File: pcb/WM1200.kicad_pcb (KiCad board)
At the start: 2 copper layers, 159 x 104 mm, 142 parts, among them Q1 BC817, Q2 BC817, Q3 BC817, Q4 BC817, Q5 BC817, Q6 BC817, U1 74LVCH162245A, U2 74LVCH162245A, U3 74LVCH162245A, U4 74LVCH162245A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

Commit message: working on pcb
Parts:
- moved X3 86.6 mm to (35.0, 118.7)
- moved XT10 77.0 mm to (189.0, 35.3)
- moved XT12 77.0 mm to (189.0, 36.8)
- moved XT14 77.0 mm to (189.0, 38.3)
- moved XT16 77.0 mm to (189.0, 39.8)
- moved XT18 77.0 mm to (189.0, 41.3)
- moved XT20 77.0 mm to (189.0, 42.8)
- moved XT6 77.0 mm to (189.0, 32.3)
- moved XT8 77.0 mm to (189.0, 33.8)
- moved U4 74.4 mm to (179.8, 42.5)
- moved XT11 73.9 mm to (170.0, 36.8)
- moved XT13 73.9 mm to (170.0, 38.3)
- moved XT15 73.9 mm to (170.0, 39.8)
- moved XT17 73.9 mm to (170.0, 41.3)
- moved XT19 73.9 mm to (170.0, 42.8)
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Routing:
- net GND: track 0.00 -> 57.5 mm
- net Net-(U5-Pad13): track 0.00 -> 19.0 mm
- net Net-(U5-Pad36): track 0.00 -> 18.9 mm, vias 0 -> 2
- net Net-(U5-Pad35): track 0.00 -> 18.8 mm, vias 0 -> 2
- net Net-(U5-Pad14): track 0.00 -> 18.6 mm
- net Net-(U5-Pad26): track 0.00 -> 9.89 mm
- net Net-(U5-Pad23): track 0.00 -> 9.85 mm
- net Net-(U5-Pad27): track 0.00 -> 8.97 mm
- net Net-(U5-Pad22): track 0.00 -> 8.90 mm
- net Net-(U5-Pad29): track 0.00 -> 8.71 mm
- net D0: track 0.00 -> 8.59 mm
- net D1: track 0.00 -> 8.57 mm
- net D2: track 0.00 -> 8.34 mm
- net D3: track 0.00 -> 8.32 mm
- net Net-(U5-Pad20): track 0.00 -> 8.32 mm
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
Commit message: working on pcb
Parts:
- moved U4 71.6 mm to (125.5, 89.2)
- moved XT11 71.6 mm to (115.8, 83.6)
- moved XT13 71.6 mm to (115.8, 85.1)
- moved XT15 71.6 mm to (115.8, 86.6)
- moved XT17 71.6 mm to (115.8, 88.1)
- moved XT19 71.6 mm to (115.8, 89.6)
- moved XT5 71.6 mm to (115.8, 79.1)
- moved XT7 71.6 mm to (115.8, 80.6)
- moved XT9 71.6 mm to (115.8, 82.1)
- moved XT10 71.6 mm to (134.8, 82.1)
- moved XT12 71.6 mm to (134.8, 83.6)
- moved XT14 71.6 mm to (134.8, 85.1)
- moved XT16 71.6 mm to (134.8, 86.6)
- moved XT18 71.6 mm to (134.8, 88.1)
- moved XT20 71.6 mm to (134.8, 89.6)
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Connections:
- XT11 pad 1: R_W -> _DS
- XT12 pad 2: FPGA_R_W -> _FPGA_DS
- XT13 pad 1: _DS -> R_W
- XT14 pad 2: _FPGA_DS -> FPGA_R_W
- XT17 pad 1: SIZE0 -> SIZE1
- XT18 pad 2: FPGA_SIZE0 -> FPGA_SIZE1
- XT19 pad 1: SIZE1 -> SIZE0
- XT20 pad 2: FPGA_SIZE1 -> FPGA_SIZE0
- XT37 pad 1: _IPL2 -> _IPL1
- XT38 pad 2: _FPGA_IPL2 -> _FPGA_IPL1
- XT39 pad 1: _IPL1 -> _IPL2
- XT40 pad 2: _FPGA_IPL1 -> _FPGA_IPL2
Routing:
- net _KBRESET: track 0.00 -> 25.7 mm
- net D18: track 0.00 -> 19.7 mm
- net A6: track 0.00 -> 19.6 mm
- net D24: track 0.00 -> 19.5 mm
- net D28: track 0.00 -> 19.3 mm
- net D8: track 0.00 -> 19.3 mm
- net D22: track 0.00 -> 19.2 mm
- net A18: track 0.00 -> 19.2 mm
- net D12: track 0.00 -> 19.1 mm
- net A2: track 0.00 -> 19.1 mm
- net A22: track 0.00 -> 19.0 mm
- net A12: track 0.00 -> 19.0 mm
- net A8: track 0.00 -> 18.9 mm
- net FC1: track 0.00 -> 13.9 mm
- net _DS: track 0.00 -> 13.0 mm
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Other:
- copper layers 2 -> 4

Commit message: Board pcb updated
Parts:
- removed XT1, XT2, XT3, XT4: testpoint, WM1200:testpoint
- removed XT53, XT54: testpoint_cutline, WM1200:testpoint_cutline
- C1, C2, C5, C9, R3, R4, R5, R6: moved to B.Cu
- C10, C3, C4, C7: value 10uF 35V -> 1uF 35V; footprint Capacitor_SMD:C_1210_3225Metric_Pad1.42x2.65mm_HandSolder -> Capacitor_SMD:C_0805_2012Metric_Pad1.15x1.40mm_HandSolder; moved to B.Cu
- C8: value 10uF 35V -> 1uF 35V; footprint Capacitor_SMD:C_1210_3225Metric_Pad1.42x2.65mm_HandSolder -> Capacitor_SMD:C_0805_2012Metric_Pad1.15x1.40mm_HandSolder
- moved XT55 222.5 mm to (120.8, 125.7)
- moved U6 221.6 mm to (125.7, 126.7)
- moved C11 212.4 mm to (125.2, 131.7), turned to 270 degrees
- moved C12 210.9 mm to (130.3, 129.6), turned to 270 degrees
- moved L1 204.1 mm to (130.3, 125.7)
- moved JP2 201.1 mm to (165.1, 58.3), turned to 90 degrees
- moved JP1 194.8 mm to (137.0, 129.2), turned to 180 degrees
- moved C6 152.2 mm to (125.6, 81.8)
- moved C8 150.8 mm to (125.6, 80.0)
- moved R1 120.0 mm to (131.2, 98.5), turned to 180 degrees
- moved C4 116.5 mm to (133.7, 105.9), turned to 180 degrees
- moved C3 107.6 mm to (133.7, 119.9), turned to 180 degrees
- moved C5 100.4 mm to (133.5, 133.3), turned to 180 degrees
- moved R2 96.3 mm to (131.2, 96.5), turned to 180 degrees
- moved C7 95.9 mm to (133.7, 135.3), turned to 180 degrees
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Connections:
- Q1 pad 3: _HLT -> Net-(Q1-Pad3)
- Q2 pad 3: _BOSS -> Net-(Q2-Pad3)
- Q3 pad 3: _INT6 -> Net-(Q3-Pad3)
- Q4 pad 3: _RST -> Net-(Q4-Pad3)
- Q5 pad 3: _INT2 -> Net-(Q5-Pad3)
- Q6 pad 3: _OVR -> Net-(Q6-Pad3)
- U3 pad 24: Net-(U3-Pad24) -> FPGA_A_BUFF_DIR
- U3 pad 25: Net-(U3-Pad25) -> _FPGA_A_BUFF_OE
- U3 pad 26: Net-(U3-Pad26) -> FPGA_A8
- U3 pad 27: Net-(U3-Pad27) -> FPGA_A9
- U3 pad 29: Net-(U3-Pad29) -> FPGA_A10
- U3 pad 30: Net-(U3-Pad30) -> FPGA_A11
- U3 pad 32: Net-(U3-Pad32) -> FPGA_A12
- U3 pad 33: Net-(U3-Pad33) -> FPGA_A13
- U3 pad 35: Net-(U3-Pad35) -> FPGA_A14
- U3 pad 36: Net-(U3-Pad36) -> FPGA_A15
- U5 pad 1: Net-(U5-Pad1) -> FPGA_INONLY_BUFF_DIR
- U5 pad 48: Net-(U5-Pad48) -> _FPGA_INONLY_BUFF_OE
- XT56 pad 1: _HLT -> Net-(Q1-Pad3)
- XT58 pad 1: _BOSS -> Net-(Q2-Pad3)
- XT60 pad 1: _INT6 -> Net-(Q3-Pad3)
- XT62 pad 1: _RST -> Net-(Q4-Pad3)
- XT64 pad 1: _INT2 -> Net-(Q5-Pad3)
- XT66 pad 1: _OVR -> Net-(Q6-Pad3)
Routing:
- net AUDIO_GND: track 0.00 -> 54.0 mm
- net AUDIO_RIGHT: track 0.00 -> 44.1 mm
- net AUDIO_LEFT: track 0.00 -> 42.5 mm
- net _HLT: track 13.9 -> 49.2 mm, vias 0 -> 2
- net _RST: track 8.11 -> 39.3 mm, vias 0 -> 2
- net D2: track 0.00 -> 22.5 mm, vias 0 -> 1
- net _DSACK0: track 0.00 -> 21.6 mm, vias 0 -> 1
- net D6: track 0.00 -> 20.9 mm, vias 0 -> 1
- net A20: track 0.00 -> 19.8 mm, vias 0 -> 1
- net _DSACK1: track 0.00 -> 19.0 mm, vias 0 -> 1
- net D4: track 0.00 -> 18.8 mm, vias 0 -> 1
- net D0: track 0.00 -> 18.6 mm
- net A7: track 0.00 -> 18.2 mm, vias 0 -> 1
- net D20: track 0.00 -> 18.0 mm, vias 0 -> 1
- net D16: track 0.00 -> 17.7 mm, vias 0 -> 1
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
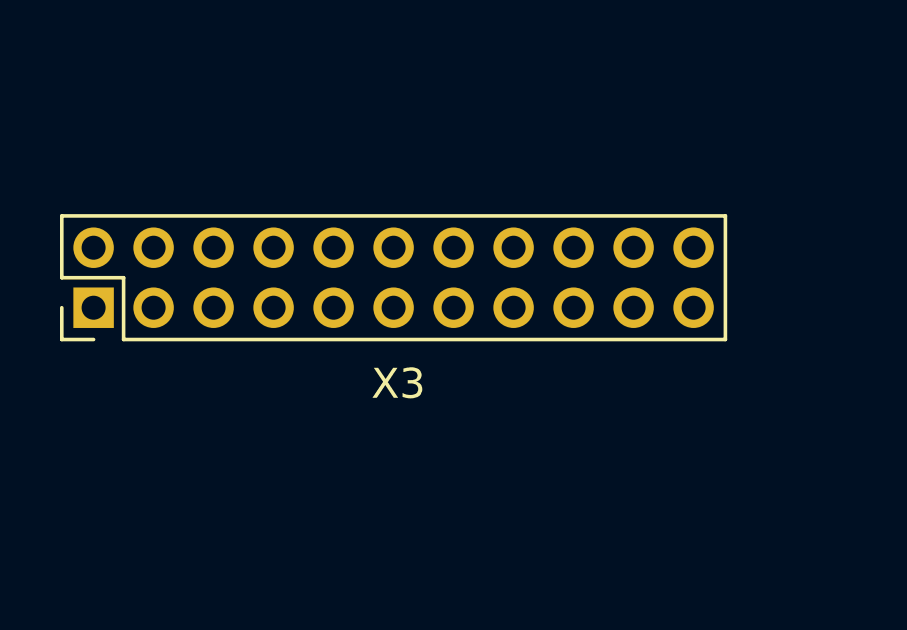
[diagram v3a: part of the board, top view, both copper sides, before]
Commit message: clockport removed from ES1 pcb design (maybe another time)
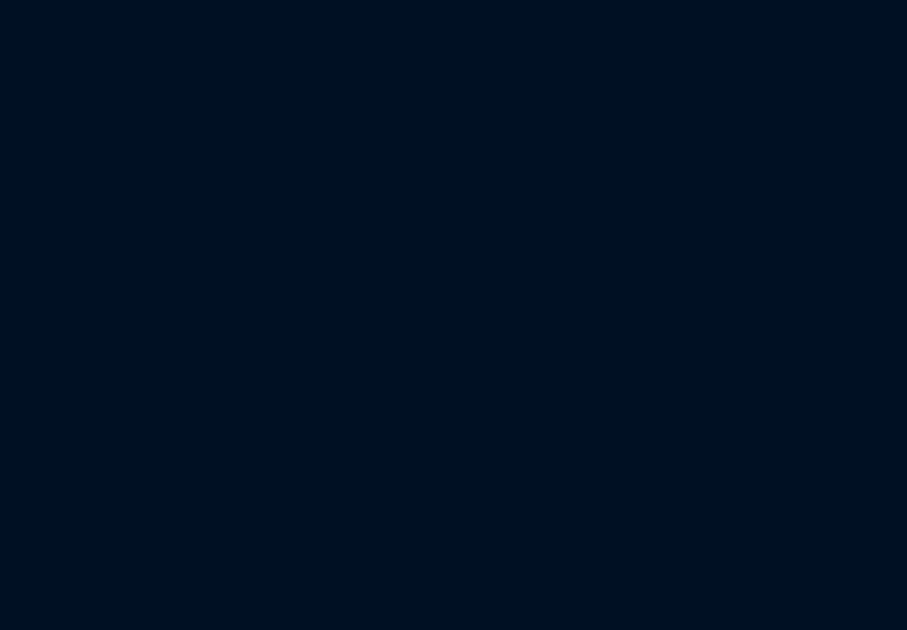
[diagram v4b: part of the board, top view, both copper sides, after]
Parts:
- removed X3: clockport_connector, WM1200:clockport
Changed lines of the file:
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@@
     (tracks 842)
     (zones 0)
-    (modules 136)
-    (nets 320)
+    (modules 135)
+    (nets 319)
   )
   (page A4)
@@
   (net 311 "Net-(U4-Pad3)")
   (net 312 "Net-(U4-Pad2)")
-  (net 313 "Net-(X3-Pad24)")
-  (net 314 "Net-(Q1-Pad3)")
-  (net 315 "Net-(Q2-Pad3)")
-  (net 316 "Net-(Q3-Pad3)")
-  (net 317 "Net-(Q4-Pad3)")
-  (net 318 "Net-(Q5-Pad3)")
-  (net 319 "Net-(Q6-Pad3)")
+  (net 313 "Net-(Q1-Pad3)")
+  (net 314 "Net-(Q2-Pad3)")
+  (net 315 "Net-(Q3-Pad3)")
+  (net 316 "Net-(Q4-Pad3)")
+  (net 317 "Net-(Q5-Pad3)")
+  (net 318 "Net-(Q6-Pad3)")
   (net_class Default "This is the default net class."
     (clearance 0.2)
@@
     (add_net "Net-(X2-Pad95)")
     (add_net "Net-(X2-Pad96)")
-    (add_net "Net-(X3-Pad24)")
     (add_net "Net-(X6-Pad14)")
     (add_net R_W)
@@
     )
   )
-  (module WM1200:clockport (layer F.Cu)
-    (at 55.35 131.7)
-    (fp_text reference X3 (at 10.16 2.54) (layer F.SilkS)
-      (effects (font (size 1 1) (thickness 0.15)))
-    )
-    (fp_text value clockport_connector (at 10.16 -5.08) (layer F.Fab)
-      (effects (font (size 1 1) (thickness 0.15)))
-    )
-    (fp_line (start 0 1) (end 21 1) (layer F.Fab) (width 0.1))
-    (fp_line (start 1 1.06) (end 21.06 1.06) (layer F.SilkS) (width 0.12))
-    (fp_line (start 21 1) (end 21 -3) (layer F.Fab) (width 0.1))
-    (fp_line (start -1.06 -3.06) (end -1.06 -1) (layer F.SilkS) (width 0.12))
-    (fp_line (start -1 0) (end 0 1) (layer F.Fab) (width 0.1))
-    (fp_line (start -1.06 -3.06) (end 21.06 -3.06) (layer F.SilkS) (width 0.12))
-    (fp_line (start 1 -1) (end 1 1.06) (layer F.SilkS) (width 0.12))
-    (fp_line (start -1.06 -1) (end 1 -1) (layer F.SilkS) (width 0.12))
-    (fp_line (start -1.06 1.06) (end 0 1.06) (layer F.SilkS) (width 0.12))
-    (fp_line (start 21 -3) (end -1 -3) (layer F.Fab) (width 0.1))
-    (fp_line (start -1.5 -3.5) (end -1.5 1.5) (layer F.CrtYd) (width 0.05))
-    (fp_line (start 21.5 1.5) (end 21.5 -3.5) (layer F.CrtYd) (width 0.05))
-    (fp_line (start 21.5 -3.5) (end -1.5 -3.5) (layer F.CrtYd) (width 0.05))
-    (fp_line (start 21.06 -3.06) (end 21.06 1.06) (layer F.SilkS) (width 0.12))
-    (fp_line (start -1.06 0) (end -1.06 1.06) (layer F.SilkS) (width 0.12))
-    (fp_line (start -1 -3) (end -1 0) (layer F.Fab) (width 0.1))
-    (fp_line (start -1.5 1.5) (end 21.5 1.5) (layer F.CrtYd) (width 0.05))
-    (pad 28 thru_hole oval (at 8 -2 90) (size 1.35 1.35) (drill 0.8) (layers *.Cu *.Mask)
-      (net 147 A4))
-    (pad 23 thru_hole oval (at 4 0 90) (size 1.35 1.35) (drill 0.8) (layers *.Cu *.Mask)
-      (net 222 _RTCCS))
-    (pad 29 thru_hole oval (at 10 0 90) (size 1.35 1.35) (drill 0.8) (layers *.Cu *.Mask)
-      (net 146 A3))
-    (pad 37 thru_hole oval (at 18 0 90) (size 1.35 1.35) (drill 0.8) (layers *.Cu *.Mask)
-      (net 56 D17))
-    (pad 33 thru_hole oval (at 14 0 90) (size 1.35 1.35) (drill 0.8) (layers *.Cu *.Mask)
-      (net 60 D21))
-    (pad 36 thru_hole oval (at 16 -2 90) (size 1.35 1.35) (drill 0.8) (layers *.Cu *.Mask)
-      (net 57 D18))
-    (pad 30 thru_hole oval (at 10 -2 90) (size 1.35 1.35) (drill 0.8) (layers *.Cu *.Mask)
-      (net 145 A2))
-    (pad 20 thru_hole oval (at 0 -2 90) (size 1.35 1.35) (drill 0.8) (layers *.Cu *.Mask)
-      (net 21 +5VDC))
-    (pad 38 thru_hole oval (at 18 -2 90) (size 1.35 1.35) (drill 0.8) (layers *.Cu *.Mask)
-      (net 55 D16))
-    (pad 21 thru_hole oval (at 2 0 90) (size 1.35 1.35) (drill 0.8) (layers *.Cu *.Mask)
-      (net 25 _INT6))
-    (pad 31 thru_hole oval (at 12 0 90) (size 1.35 1.35) (drill 0.8) (layers *.Cu *.Mask)
-      (net 62 D23))
-    (pad 35 thru_hole oval (at 16 0 90) (size 1.35 1.35) (drill 0.8) (layers *.Cu *.Mask)
-      (net 58 D19))
-    (pad 32 thru_hole oval (at 12 -2 90) (size 1.35 1.35) (drill 0.8) (layers *.Cu *.Mask)
-      (net 61 D22))
-    (pad 19 thru_hole rect (at 0 0 90) (size 1.35 1.35) (drill 0.8) (layers *.Cu *.Mask)
-      (net 2 GND))
-    (pad 39 thru_hole oval (at 20 0 90) (size 1.35 1.35) (drill 0.8) (layers *.Cu *.Mask)
-      (net 2 GND))
-    (pad 26 thru_hole oval (at 6 -2 90) (size 1.35 1.35) (drill 0.8) (layers *.Cu *.Mask)
-      (net 215 _IOWR))
-    (pad 25 thru_hole oval (at 6 0 90) (size 1.35 1.35) (drill 0.8) (layers *.Cu *.Mask)
-      (net 216 _IORD))
-    (pad 34 thru_hole oval (at 14 -2 90) (size 1.35 1.35) (drill 0.8) (layers *.Cu *.Mask)
-      (net 59 D20))
-    (pad 22 thru_hole oval (at 2 -2 90) (size 1.35 1.35) (drill 0.8) (layers *.Cu *.Mask)
-      (net 223 _SPARECS))
-    (pad 40 thru_hole oval (at 20 -2 90) (size 1.35 1.35) (drill 0.8) (layers *.Cu *.Mask)
-      (net 225 _RESET))
-    (pad 24 thru_hole oval (at 4 -2 90) (size 1.35 1.35) (drill 0.8) (layers *.Cu *.Mask)
-      (net 313 "Net-(X3-Pad24)"))
-    (pad 27 thru_hole oval (at 8 0 90) (size 1.35 1.35) (drill 0.8) (layers *.Cu *.Mask)
-      (net 148 A5))
-    (model ${KISYS3DMOD}/Connector_PinHeader_2.00mm.3dshapes/PinHeader_2x11_P2.00mm_Vertical.step
-      (at (xyz 0 0 0))
-      (scale (xyz 1 1 1))
-      (rotate (xyz 0 0 -90))
-    )
-  )
   (module Connector_PinHeader_2.54mm:PinHeader_2x06_P2.54mm_Vertical (layer F.Cu)
     (at 145.94 65.85 180)
@@
       (net 28 _OVR))
     (pad 1 smd roundrect (at -0.5 1.905 180) (size 1 1) (layers F.Cu F.Paste F.Mask) (roundrect_rratio 0.25)
-      (net 319 "Net-(Q6-Pad3)"))
+      (net 318 "Net-(Q6-Pad3)"))
   )
   (module WM1200:testpoint_cutline (layer F.Cu)
@@
       (net 27 _INT2))
     (pad 1 smd roundrect (at -0.5 1.905 180) (size 1 1) (layers F.Cu F.Paste F.Mask) (roundrect_rratio 0.25)
-      (net 318 "Net-(Q5-Pad3)"))
+      (net 317 "Net-(Q5-Pad3)"))
   )
   (module WM1200:testpoint_cutline (layer F.Cu)
@@
       (net 26 _RST))
     (pad 1 smd roundrect (at -0.5 1.905 180) (size 1 1) (layers F.Cu F.Paste F.Mask) (roundrect_rratio 0.25)
-      (net 317 "Net-(Q4-Pad3)"))
+      (net 316 "Net-(Q4-Pad3)"))
   )
   (module WM1200:testpoint_cutline (layer F.Cu)
@@
       (net 25 _INT6))
     (pad 1 smd roundrect (at -0.5 1.905 180) (size 1 1) (layers F.Cu F.Paste F.Mask) (roundrect_rratio 0.25)
-      (net 316 "Net-(Q3-Pad3)"))
+      (net 315 "Net-(Q3-Pad3)"))
   )
   (module WM1200:testpoint_cutline (layer F.Cu)
@@
       (net 24 _BOSS))
     (pad 1 smd roundrect (at -0.5 1.905 180) (size 1 1) (layers F.Cu F.Paste F.Mask) (roundrect_rratio 0.25)
-      (net 315 "Net-(Q2-Pad3)"))
+      (net 314 "Net-(Q2-Pad3)"))
   )
   (module WM1200:testpoint_cutline (layer F.Cu)
@@
       (net 23 _HLT))
     (pad 1 smd roundrect (at -0.5 1.905 180) (size 1 1) (layers F.Cu F.Paste F.Mask) (roundrect_rratio 0.25)
-      (net 314 "Net-(Q1-Pad3)"))
+      (net 313 "Net-(Q1-Pad3)"))
   )
   (module WM1200:testpoint_cutline (layer F.Cu)
@@
     )
     (pad 3 smd rect (at 1 0 180) (size 0.9 0.8) (layers F.Cu F.Paste F.Mask)
-      (net 319 "Net-(Q6-Pad3)"))
+      (net 318 "Net-(Q6-Pad3)"))
     (pad 2 smd rect (at -1 0.95 180) (size 0.9 0.8) (layers F.Cu F.Paste F.Mask)
       (net 2 GND))
@@
     )
     (pad 3 smd rect (at 1 0 180) (size 0.9 0.8) (layers F.Cu F.Paste F.Mask)
-      (net 318 "Net-(Q5-Pad3)"))
+      (net 317 "Net-(Q5-Pad3)"))
     (pad 2 smd rect (at -1 0.95 180) (size 0.9 0.8) (layers F.Cu F.Paste F.Mask)
       (net 2 GND))
@@
     )
     (pad 3 smd rect (at 1 0 180) (size 0.9 0.8) (layers F.Cu F.Paste F.Mask)
-      (net 317 "Net-(Q4-Pad3)"))
+      (net 316 "Net-(Q4-Pad3)"))
     (pad 2 smd rect (at -1 0.95 180) (size 0.9 0.8) (layers F.Cu F.Paste F.Mask)
       (net 2 GND))
@@
     )
     (pad 3 smd rect (at 1 0 180) (size 0.9 0.8) (layers F.Cu F.Paste F.Mask)
-      (net 316 "Net-(Q3-Pad3)"))
+      (net 315 "Net-(Q3-Pad3)"))
     (pad 2 smd rect (at -1 0.95 180) (size 0.9 0.8) (layers F.Cu F.Paste F.Mask)
       (net 2 GND))
@@
     )
     (pad 3 smd rect (at 1 0 180) (size 0.9 0.8) (layers F.Cu F.Paste F.Mask)
-      (net 315 "Net-(Q2-Pad3)"))
+      (net 314 "Net-(Q2-Pad3)"))
     (pad 2 smd rect (at -1 0.95 180) (size 0.9 0.8) (layers F.Cu F.Paste F.Mask)
       (net 2 GND))
@@
     )
     (pad 3 smd rect (at 1 0 180) (size 0.9 0.8) (layers F.Cu F.Paste F.Mask)
-      (net 314 "Net-(Q1-Pad3)"))
+      (net 313 "Net-(Q1-Pad3)"))
     (pad 2 smd rect (at -1 0.95 180) (size 0.9 0.8) (layers F.Cu F.Paste F.Mask)
       (net 2 GND))
@@
   (segment (start 120.3 84) (end 121.05 84) (width 0.25) (layer F.Cu) (net 312))
   (segment (start 116.8 81) (end 117.3 81) (width 0.25) (layer F.Cu) (net 312))
-  (segment (start 120.3 111) (end 118.3 111) (width 0.25) (layer F.Cu) (net 314))
-  (segment (start 120.3 75.85) (end 118.3 75.85) (width 0.25) (layer F.Cu) (net 315))
-  (segment (start 120.3 62.1) (end 118.3 62.1) (width 0.25) (layer F.Cu) (net 316))
-  (segment (start 120.3 103.25) (end 118.3 103.25) (width 0.25) (layer F.Cu) (net 317))
-  (segment (start 120.3 55.2) (end 118.3 55.2) (width 0.25) (layer F.Cu) (net 318))
-  (segment (start 120.3 69) (end 118.3 69) (width 0.25) (layer F.Cu) (net 319))
+  (segment (start 120.3 111) (end 118.3 111) (width 0.25) (layer F.Cu) (net 313))
+  (segment (start 120.3 75.85) (end 118.3 75.85) (width 0.25) (layer F.Cu) (net 314))
+  (segment (start 120.3 62.1) (end 118.3 62.1) (width 0.25) (layer F.Cu) (net 315))
+  (segment (start 120.3 103.25) (end 118.3 103.25) (width 0.25) (layer F.Cu) (net 316))
+  (segment (start 120.3 55.2) (end 118.3 55.2) (width 0.25) (layer F.Cu) (net 317))
+  (segment (start 120.3 69) (end 118.3 69) (width 0.25) (layer F.Cu) (net 318))
 )

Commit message: Ground plane added
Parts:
- moved XT62 2.00 mm to (115.8, 105.2)
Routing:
- net GND: track 57.5 -> 69.3 mm, vias 0 -> 7
- net _RST: track 39.3 -> 37.3 mm
- net Net-(Q4-Pad3): track 2.00 -> 4.00 mm
- added copper zone on In2.Cu, net +5VDC
- added copper zone on In1.Cu, net GND
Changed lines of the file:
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@@
     (thickness 1.6)
     (drawings 10)
-    (tracks 842)
+    (tracks 856)
     (zones 0)
     (modules 135)
@@
     (last_trace_width 0.25)
     (trace_clearance 0.2)
-    (zone_clearance 0.508)
+    (zone_clearance 0.3)
     (zone_45_only no)
     (trace_min 0.2)
@@
   )
   (module WM1200:testpoint_cutline (layer F.Cu)
-    (at 117.8 105.155 180)
+    (at 115.8 105.155 180)
     (fp_text reference XT62 (at 0 0.5) (layer F.SilkS)
       (effects (font (size 1 1) (thickness 0.15)))
@@
   (segment (start 126.9 53.2) (end 126.3 53.8) (width 0.25) (layer F.Cu) (net 2))
   (segment (start 129.95 53.2) (end 126.9 53.2) (width 0.25) (layer F.Cu) (net 2))
+  (via micro (at 123.5 90.5) (size 0.3) (drill 0.1) (layers F.Cu In1.Cu) (net 2))
+  (segment (start 121.8 90.5) (end 123.5 90.5) (width 0.25) (layer F.Cu) (net 2))
+  (via micro (at 123.5 93.5) (size 0.3) (drill 0.1) (layers F.Cu In1.Cu) (net 2))
+  (segment (start 121.8 93.5) (end 123.5 93.5) (width 0.25) (layer F.Cu) (net 2))
+  (via micro (at 127.6 93.5) (size 0.3) (drill 0.1) (layers F.Cu In1.Cu) (net 2))
+  (segment (start 129.3 93.5) (end 127.6 93.5) (width 0.25) (layer F.Cu) (net 2))
+  (segment (start 129.3 90.5) (end 127.6 90.5) (width 0.25) (layer F.Cu) (net 2))
+  (via micro (at 127.6 90.5) (size 0.3) (drill 0.1) (layers F.Cu In1.Cu) (net 2))
+  (via micro (at 127.6 88) (size 0.3) (drill 0.1) (layers F.Cu In1.Cu) (net 2))
+  (segment (start 129.3 88) (end 127.6 88) (width 0.25) (layer F.Cu) (net 2))
+  (via micro (at 127.6 85) (size 0.3) (drill 0.1) (layers F.Cu In1.Cu) (net 2))
+  (segment (start 129.3 85) (end 127.6 85) (width 0.25) (layer F.Cu) (net 2))
+  (via micro (at 123.4 85) (size 0.3) (drill 0.1) (layers F.Cu In1.Cu) (net 2))
+  (segment (start 121.8 85) (end 123.4 85) (width 0.25) (layer F.Cu) (net 2))
   (segment (start 124.4 127.6) (end 124.425001 127.625001) (width 0.25) (layer F.Cu) (net 3))
   (segment (start 123 126.290002) (end 123 127.6) (width 0.3) (layer F.Cu) (net 3))
@@
   (segment (start 107.278762 103.05) (end 107.911238 103.05) (width 0.25) (layer In2.Cu) (net 26))
   (segment (start 107.911238 103.05) (end 108.978239 101.982999) (width 0.25) (layer In2.Cu) (net 26))
-  (segment (start 112.3 103.25) (end 116.8 103.25) (width 0.25) (layer F.Cu) (net 26))
+  (segment (start 112.3 103.25) (end 114.8 103.25) (width 0.25) (layer F.Cu) (net 26))
   (segment (start 111.65 55.2) (end 109.5 57.35) (width 0.25) (layer F.Cu) (net 27))
   (segment (start 116.8 55.2) (end 111.65 55.2) (width 0.25) (layer F.Cu) (net 27))
@@
   (segment (start 120.3 75.85) (end 118.3 75.85) (width 0.25) (layer F.Cu) (net 314))
   (segment (start 120.3 62.1) (end 118.3 62.1) (width 0.25) (layer F.Cu) (net 315))
-  (segment (start 120.3 103.25) (end 118.3 103.25) (width 0.25) (layer F.Cu) (net 316))
+  (segment (start 120.3 103.25) (end 116.3 103.25) (width 0.25) (layer F.Cu) (net 316))
   (segment (start 120.3 55.2) (end 118.3 55.2) (width 0.25) (layer F.Cu) (net 317))
   (segment (start 120.3 69) (end 118.3 69) (width 0.25) (layer F.Cu) (net 318))
+  (zone (net 2) (net_name GND) (layer In1.Cu) (hatch edge 0.508)
+    (connect_pads (clearance 0.3))
+    (min_thickness 0.2)
+    (fill yes (arc_segments 32) (thermal_gap 0.25) (thermal_bridge_width 0.3))
+    (polygon
+      (pts
+        (xy 151 74) (xy 249 74) (xy 249 150) (xy 90 150) (xy 90 46)
+        (xy 151 46)
+      )
+    )
+  )
+  (zone (net 21) (net_name +5VDC) (layer In2.Cu) (hatch edge 0.508)
+    (connect_pads (clearance 0.3))
+    (min_thickness 0.2)
+    (fill yes (arc_segments 32) (thermal_gap 0.25) (thermal_bridge_width 0.3))
+    (polygon
+      (pts
+        (xy 120 150) (xy 90 150) (xy 90 46) (xy 120 46)
+      )
+    )
+  )
 )
